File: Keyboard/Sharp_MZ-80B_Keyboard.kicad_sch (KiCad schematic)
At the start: 98 parts, among them J1 Tape Controls, J2 Keyboard Matrix, J3 LEDs, SW1 CMT_EJECT, SW10 CLR HOME, SW11 INST DEL, SW12 8, SW13 9, SW14 COLON, SW15 SEMI COLON, SW16 -, SW17 @, SW18 [, SW19 0, SW2 CMT_FF, SW20 1, SW21 2, SW22 3, SW23 4, SW24 5, SW25 6, SW26 7, SW27 X, SW28 Y, SW29 Z, SW3 CMT_REW, SW30 ^, SW31 \, SW32 ?, SW33 DOT, SW34 COMMA, SW35 P, SW36 Q, SW37 R, SW38 S, SW39 T, SW4 CMT_STOP, SW40 U, SW41 V, SW42 W, SW43 I, SW44 H, SW45 J, SW46 K, SW47 L, SW48 M, SW49 N, SW5 GRPH, SW50 O, SW51 /, SW52 A, SW53 B, SW54 C, SW55 D, SW56 E, SW57 F, SW58 G, SW59 TAB, SW6 SFT LOCK, SW60 SPACE, SW61 CR, SW62 UP, SW63 DOWN, SW64 LEFT, SW65 RIGHT, SW66 BREAK, SW67 NP 0, SW68 NP 1, SW69 NP 2, SW7 RH SHIFT, SW70 NP 3, SW71 NP 4, SW72 NP 5, SW73 NP 6, SW74 NP 7, SW75 F9, SW76 F10, SW77 NP 8, SW78 NP 9, SW79 NP 00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

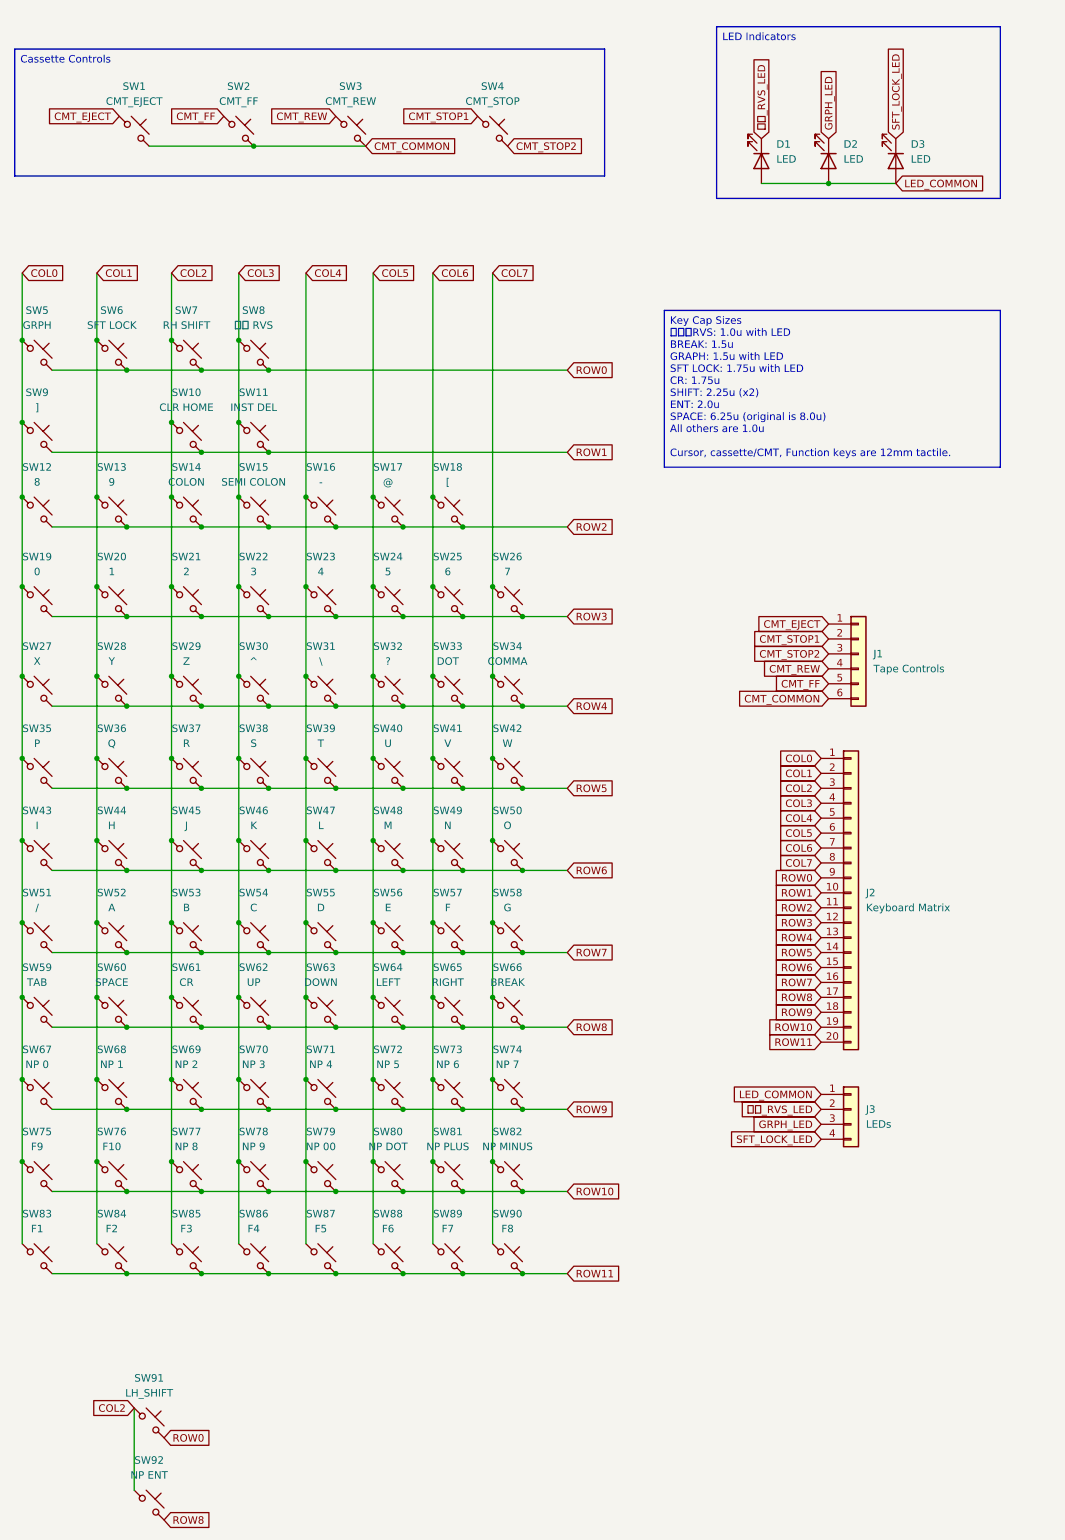
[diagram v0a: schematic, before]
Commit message: Schematic updates
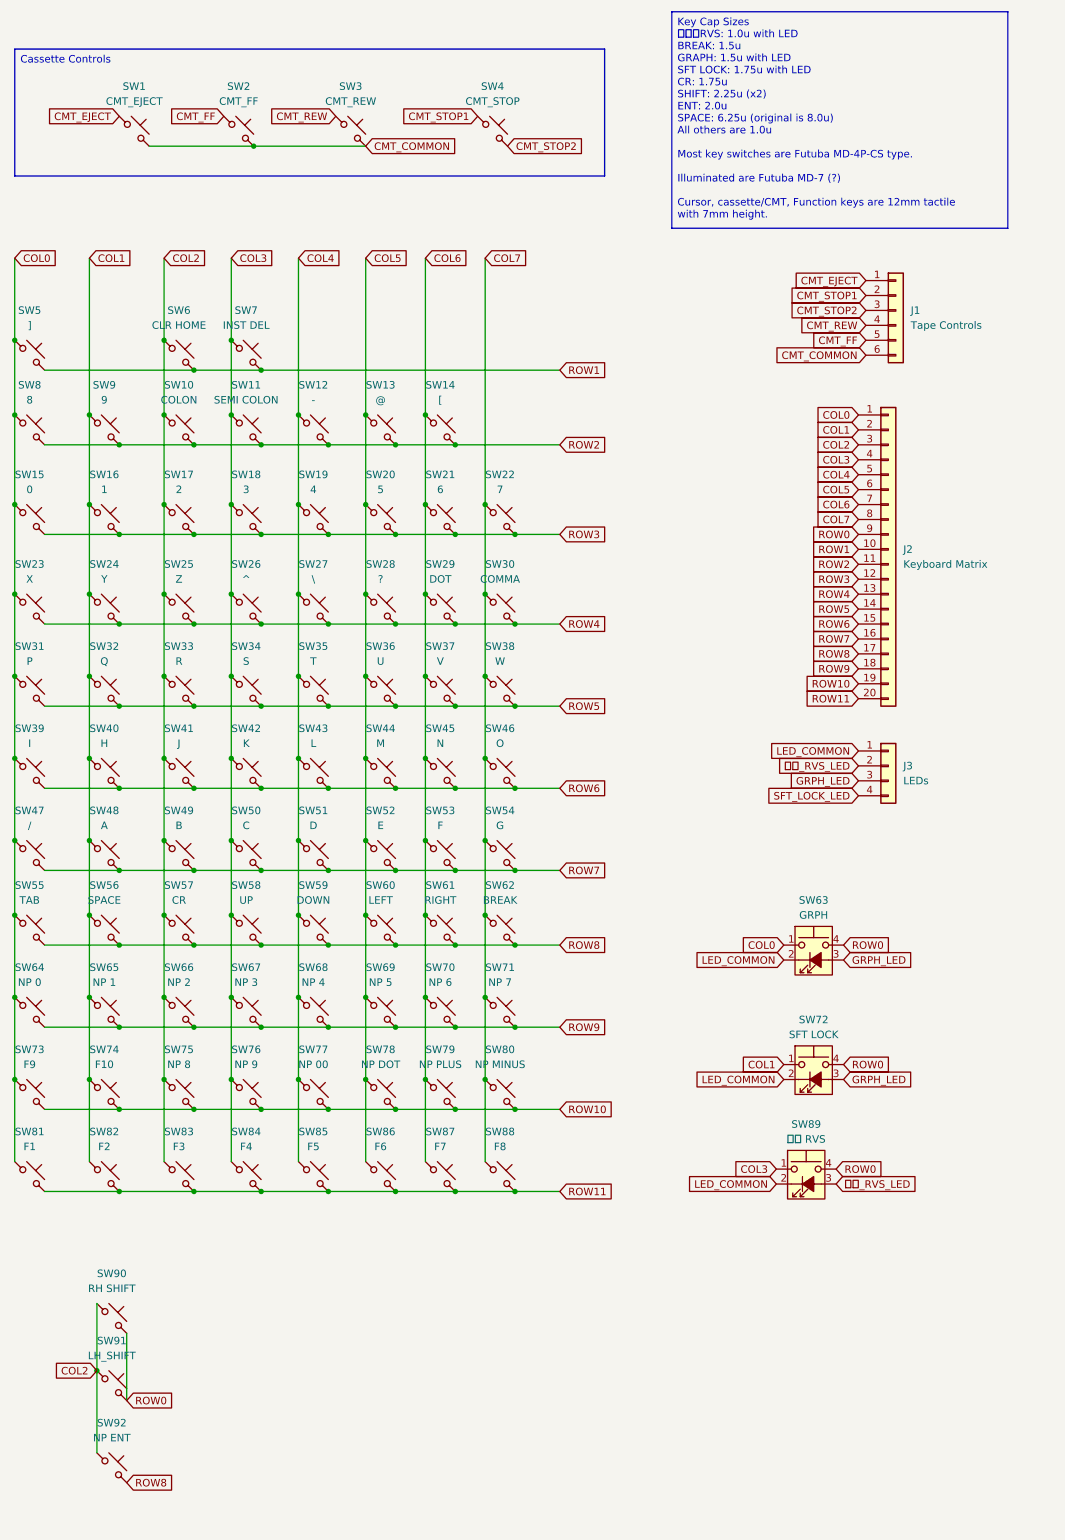
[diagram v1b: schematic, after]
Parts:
- removed D1, D2, D3: LED, LED_THT:LED_D5.0mm, symbol Device:LED
- removed SW5: GRPH, PCM_Switch_Keyboard_Cherry_MX:SW_Cherry_MX_Plate_1.50u, symbol Switch:SW_Push_45deg
- removed SW6: SFT LOCK, PCM_Switch_Keyboard_Cherry_MX:SW_Cherry_MX_Plate_1.75u, symbol Switch:SW_Push_45deg
- removed SW8: カナ RVS, PCM_Switch_Keyboard_Cherry_MX:SW_Cherry_MX_Plate_1.00u, symbol Switch:SW_Push_45deg
- added SW63: GRPH, Clueless_Engineer:Futuba MD-7, symbol Switch:SW_MEC_5G_LED
- added SW72: SFT LOCK, Clueless_Engineer:Futuba MD-7, symbol Switch:SW_MEC_5G_LED
- added SW89: カナ RVS, Clueless_Engineer:Futuba MD-7, symbol Switch:SW_MEC_5G_LED
- SW10: renamed from SW14; footprint PCM_Switch_Keyboard_Cherry_MX:SW_Cherry_MX_Plate_1.00u -> Clueless_Engineer:Futuba MD-4P
- SW11: renamed from SW15; footprint PCM_Switch_Keyboard_Cherry_MX:SW_Cherry_MX_Plate_1.00u -> Clueless_Engineer:Futuba MD-4P
- SW12: renamed from SW16; footprint PCM_Switch_Keyboard_Cherry_MX:SW_Cherry_MX_Plate_1.00u -> Clueless_Engineer:Futuba MD-4P
- SW13: renamed from SW17; footprint PCM_Switch_Keyboard_Cherry_MX:SW_Cherry_MX_Plate_1.00u -> Clueless_Engineer:Futuba MD-4P
- SW14: renamed from SW18; footprint PCM_Switch_Keyboard_Cherry_MX:SW_Cherry_MX_Plate_1.00u -> Clueless_Engineer:Futuba MD-4P
- SW15: renamed from SW19; footprint PCM_Switch_Keyboard_Cherry_MX:SW_Cherry_MX_Plate_1.00u -> Clueless_Engineer:Futuba MD-4P
- SW16: renamed from SW20; footprint PCM_Switch_Keyboard_Cherry_MX:SW_Cherry_MX_Plate_1.00u -> Clueless_Engineer:Futuba MD-4P
- SW17: renamed from SW21; footprint PCM_Switch_Keyboard_Cherry_MX:SW_Cherry_MX_Plate_1.00u -> Clueless_Engineer:Futuba MD-4P
- SW18: renamed from SW22; footprint PCM_Switch_Keyboard_Cherry_MX:SW_Cherry_MX_Plate_1.00u -> Clueless_Engineer:Futuba MD-4P
- SW19: renamed from SW23; footprint PCM_Switch_Keyboard_Cherry_MX:SW_Cherry_MX_Plate_1.00u -> Clueless_Engineer:Futuba MD-4P
- SW20: renamed from SW24; footprint PCM_Switch_Keyboard_Cherry_MX:SW_Cherry_MX_Plate_1.00u -> Clueless_Engineer:Futuba MD-4P
- SW21: renamed from SW25; footprint PCM_Switch_Keyboard_Cherry_MX:SW_Cherry_MX_Plate_1.00u -> Clueless_Engineer:Futuba MD-4P
- SW22: renamed from SW26; footprint PCM_Switch_Keyboard_Cherry_MX:SW_Cherry_MX_Plate_1.00u -> Clueless_Engineer:Futuba MD-4P
- SW23: renamed from SW27; footprint PCM_Switch_Keyboard_Cherry_MX:SW_Cherry_MX_Plate_1.00u -> Clueless_Engineer:Futuba MD-4P
- SW24: renamed from SW28; footprint PCM_Switch_Keyboard_Cherry_MX:SW_Cherry_MX_Plate_1.00u -> Clueless_Engineer:Futuba MD-4P
- SW25: renamed from SW29; footprint PCM_Switch_Keyboard_Cherry_MX:SW_Cherry_MX_Plate_1.00u -> Clueless_Engineer:Futuba MD-4P
- SW26: renamed from SW30; footprint PCM_Switch_Keyboard_Cherry_MX:SW_Cherry_MX_Plate_1.00u -> Clueless_Engineer:Futuba MD-4P
- SW27: renamed from SW31; footprint PCM_Switch_Keyboard_Cherry_MX:SW_Cherry_MX_Plate_1.00u -> Clueless_Engineer:Futuba MD-4P
- SW28: renamed from SW32; footprint PCM_Switch_Keyboard_Cherry_MX:SW_Cherry_MX_Plate_1.00u -> Clueless_Engineer:Futuba MD-4P
- SW29: renamed from SW33; footprint PCM_Switch_Keyboard_Cherry_MX:SW_Cherry_MX_Plate_1.00u -> Clueless_Engineer:Futuba MD-4P
- SW30: renamed from SW34; footprint PCM_Switch_Keyboard_Cherry_MX:SW_Cherry_MX_Plate_1.00u -> Clueless_Engineer:Futuba MD-4P
- SW31: renamed from SW35; footprint PCM_Switch_Keyboard_Cherry_MX:SW_Cherry_MX_Plate_1.00u -> Clueless_Engineer:Futuba MD-4P
- SW32: renamed from SW36; footprint PCM_Switch_Keyboard_Cherry_MX:SW_Cherry_MX_Plate_1.00u -> Clueless_Engineer:Futuba MD-4P
- SW33: renamed from SW37; footprint PCM_Switch_Keyboard_Cherry_MX:SW_Cherry_MX_Plate_1.00u -> Clueless_Engineer:Futuba MD-4P
- SW34: renamed from SW38; footprint PCM_Switch_Keyboard_Cherry_MX:SW_Cherry_MX_Plate_1.00u -> Clueless_Engineer:Futuba MD-4P
- SW35: renamed from SW39; footprint PCM_Switch_Keyboard_Cherry_MX:SW_Cherry_MX_Plate_1.00u -> Clueless_Engineer:Futuba MD-4P
- SW36: renamed from SW40; footprint PCM_Switch_Keyboard_Cherry_MX:SW_Cherry_MX_Plate_1.00u -> Clueless_Engineer:Futuba MD-4P
- SW37: renamed from SW41; footprint PCM_Switch_Keyboard_Cherry_MX:SW_Cherry_MX_Plate_1.00u -> Clueless_Engineer:Futuba MD-4P
- SW38: renamed from SW42; footprint PCM_Switch_Keyboard_Cherry_MX:SW_Cherry_MX_Plate_1.00u -> Clueless_Engineer:Futuba MD-4P
- SW39: renamed from SW43; footprint PCM_Switch_Keyboard_Cherry_MX:SW_Cherry_MX_Plate_1.00u -> Clueless_Engineer:Futuba MD-4P
- SW40: renamed from SW44; footprint PCM_Switch_Keyboard_Cherry_MX:SW_Cherry_MX_Plate_1.00u -> Clueless_Engineer:Futuba MD-4P
- SW41: renamed from SW45; footprint PCM_Switch_Keyboard_Cherry_MX:SW_Cherry_MX_Plate_1.00u -> Clueless_Engineer:Futuba MD-4P
- SW42: renamed from SW46; footprint PCM_Switch_Keyboard_Cherry_MX:SW_Cherry_MX_Plate_1.00u -> Clueless_Engineer:Futuba MD-4P
- SW43: renamed from SW47; footprint PCM_Switch_Keyboard_Cherry_MX:SW_Cherry_MX_Plate_1.00u -> Clueless_Engineer:Futuba MD-4P
- SW44: renamed from SW48; footprint PCM_Switch_Keyboard_Cherry_MX:SW_Cherry_MX_Plate_1.00u -> Clueless_Engineer:Futuba MD-4P
- SW45: renamed from SW49; footprint PCM_Switch_Keyboard_Cherry_MX:SW_Cherry_MX_Plate_1.00u -> Clueless_Engineer:Futuba MD-4P
- SW46: renamed from SW50; footprint PCM_Switch_Keyboard_Cherry_MX:SW_Cherry_MX_Plate_1.00u -> Clueless_Engineer:Futuba MD-4P
- SW47: renamed from SW51; footprint PCM_Switch_Keyboard_Cherry_MX:SW_Cherry_MX_Plate_1.00u -> Clueless_Engineer:Futuba MD-4P
- SW48: renamed from SW52; footprint PCM_Switch_Keyboard_Cherry_MX:SW_Cherry_MX_Plate_1.00u -> Clueless_Engineer:Futuba MD-4P
- SW49: renamed from SW53; footprint PCM_Switch_Keyboard_Cherry_MX:SW_Cherry_MX_Plate_1.00u -> Clueless_Engineer:Futuba MD-4P
- SW5: renamed from SW9; footprint PCM_Switch_Keyboard_Cherry_MX:SW_Cherry_MX_Plate_1.00u -> Clueless_Engineer:Futuba MD-4P
- SW50: renamed from SW54; footprint PCM_Switch_Keyboard_Cherry_MX:SW_Cherry_MX_Plate_1.00u -> Clueless_Engineer:Futuba MD-4P
- SW51: renamed from SW55; footprint PCM_Switch_Keyboard_Cherry_MX:SW_Cherry_MX_Plate_1.00u -> Clueless_Engineer:Futuba MD-4P
- SW52: renamed from SW56; footprint PCM_Switch_Keyboard_Cherry_MX:SW_Cherry_MX_Plate_1.00u -> Clueless_Engineer:Futuba MD-4P
- SW53: renamed from SW57; footprint PCM_Switch_Keyboard_Cherry_MX:SW_Cherry_MX_Plate_1.00u -> Clueless_Engineer:Futuba MD-4P
- SW54: renamed from SW58; footprint PCM_Switch_Keyboard_Cherry_MX:SW_Cherry_MX_Plate_1.00u -> Clueless_Engineer:Futuba MD-4P
- SW55: renamed from SW59; footprint PCM_Switch_Keyboard_Cherry_MX:SW_Cherry_MX_Plate_1.00u -> Clueless_Engineer:Futuba MD-4P
- SW56: renamed from SW60; footprint PCM_Switch_Keyboard_Cherry_MX:SW_Cherry_MX_Plate_6.25u -> Clueless_Engineer:Futuba MD-4P
- SW57: renamed from SW61; footprint PCM_Switch_Keyboard_Cherry_MX:SW_Cherry_MX_Plate_1.75u -> Clueless_Engineer:Futuba MD-4P
- SW6: renamed from SW10; footprint PCM_Switch_Keyboard_Cherry_MX:SW_Cherry_MX_Plate_1.00u -> Clueless_Engineer:Futuba MD-4P
- SW62: renamed from SW66; footprint PCM_Switch_Keyboard_Cherry_MX:SW_Cherry_MX_Plate_1.50u -> Clueless_Engineer:Futuba MD-4P
- SW64: renamed from SW67; footprint PCM_Switch_Keyboard_Cherry_MX:SW_Cherry_MX_Plate_1.00u -> Clueless_Engineer:Futuba MD-4P
- SW65: renamed from SW68; footprint PCM_Switch_Keyboard_Cherry_MX:SW_Cherry_MX_Plate_1.00u -> Clueless_Engineer:Futuba MD-4P
- SW66: renamed from SW69; footprint PCM_Switch_Keyboard_Cherry_MX:SW_Cherry_MX_Plate_1.00u -> Clueless_Engineer:Futuba MD-4P
- SW67: renamed from SW70; footprint PCM_Switch_Keyboard_Cherry_MX:SW_Cherry_MX_Plate_1.00u -> Clueless_Engineer:Futuba MD-4P
- SW68: renamed from SW71; footprint PCM_Switch_Keyboard_Cherry_MX:SW_Cherry_MX_Plate_1.00u -> Clueless_Engineer:Futuba MD-4P
- SW69: renamed from SW72; footprint PCM_Switch_Keyboard_Cherry_MX:SW_Cherry_MX_Plate_1.00u -> Clueless_Engineer:Futuba MD-4P
- SW7: renamed from SW11; footprint PCM_Switch_Keyboard_Cherry_MX:SW_Cherry_MX_Plate_1.00u -> Clueless_Engineer:Futuba MD-4P
- SW70: renamed from SW73; footprint PCM_Switch_Keyboard_Cherry_MX:SW_Cherry_MX_Plate_1.00u -> Clueless_Engineer:Futuba MD-4P
- SW71: renamed from SW74; footprint PCM_Switch_Keyboard_Cherry_MX:SW_Cherry_MX_Plate_1.00u -> Clueless_Engineer:Futuba MD-4P
- SW75: renamed from SW77; footprint PCM_Switch_Keyboard_Cherry_MX:SW_Cherry_MX_Plate_1.00u -> Clueless_Engineer:Futuba MD-4P
- SW76: renamed from SW78; footprint PCM_Switch_Keyboard_Cherry_MX:SW_Cherry_MX_Plate_1.00u -> Clueless_Engineer:Futuba MD-4P
- SW77: renamed from SW79; footprint PCM_Switch_Keyboard_Cherry_MX:SW_Cherry_MX_Plate_1.00u -> Clueless_Engineer:Futuba MD-4P
- SW78: renamed from SW80; footprint PCM_Switch_Keyboard_Cherry_MX:SW_Cherry_MX_Plate_1.00u -> Clueless_Engineer:Futuba MD-4P
- SW79: renamed from SW81; footprint PCM_Switch_Keyboard_Cherry_MX:SW_Cherry_MX_Plate_1.00u -> Clueless_Engineer:Futuba MD-4P
- SW8: renamed from SW12; footprint PCM_Switch_Keyboard_Cherry_MX:SW_Cherry_MX_Plate_1.00u -> Clueless_Engineer:Futuba MD-4P
- SW80: renamed from SW82; footprint PCM_Switch_Keyboard_Cherry_MX:SW_Cherry_MX_Plate_1.00u -> Clueless_Engineer:Futuba MD-4P
- SW9: renamed from SW13; footprint PCM_Switch_Keyboard_Cherry_MX:SW_Cherry_MX_Plate_1.00u -> Clueless_Engineer:Futuba MD-4P
- SW90: renamed from SW7; footprint PCM_Switch_Keyboard_Cherry_MX:SW_Cherry_MX_Plate_2.25u -> Clueless_Engineer:Futuba MD-4P
- SW91: footprint PCM_Switch_Keyboard_Cherry_MX:SW_Cherry_MX_Plate_2.25u -> Clueless_Engineer:Futuba MD-4P
- SW92: footprint PCM_Switch_Keyboard_Cherry_MX:SW_Cherry_MX_Plate_2.00u_90deg -> Clueless_Engineer:Futuba MD-4P
- renumbered SW62 to SW58, SW63 to SW59, SW64 to SW60, SW65 to SW61, SW75 to SW73, SW76 to SW74, SW83 to SW81, SW84 to SW82, SW85 to SW83, SW86 to SW84, SW87 to SW85, SW88 to SW86, SW89 to SW87, SW90 to SW88
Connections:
- net COL0: now also SW63.1
- net COL1: now also SW72.1
- net COL3: now also SW89.1
- net GRPH_LED: now also SW63.3 (K), SW72.3 (K)
- net LED_COMMON: now also SW63.2, SW72.2, SW89.2
- net ROW0: now also SW63.4 (A), SW72.4 (A), SW89.4 (A)
- net カナ_RVS_LED: now also SW89.3 (K)
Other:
- moved on the sheet: J1, J2, J3, SW10, SW11, SW12, SW13, SW14, SW15, SW16, SW17, SW18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

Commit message: Initial design
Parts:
- SW15: value 0 -> ZERO
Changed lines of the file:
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@@
 		)
 	)
-	(text_box "Key Cap Sizes\nカナ　RVS: 1.0u with LED\nBREAK: 1.5u\nGRAPH: 1.5u with LED\nSFT LOCK: 1.75u with LED\nCR: 1.75u\nSHIFT: 2.25u (x2)\nENT: 2.0u\nSPACE: 6.25u (original is 8.0u)\nAll others are 1.0u\n\nMost key switches are Futuba MD-4P-CS type.\n\nIlluminated are Futuba MD-7 (?)\n\nCursor, cassette/CMT, Function keys are 12mm tactile with 7mm height."
+	(text_box "Key Cap Sizes\nカナ　RVS: 1.0u with LED\nBREAK: 1.5u\nGRAPH: 1.5u with LED\nSFT LOCK: 1.75u with LED\nCR: 1.75u\nSHIFT: 2.25u (x2)\nENT: 2.0u\nSPACE: 8.0u\nAll others are 1.0u\n\nMost key switches are Futuba MD-4P-CS type.\n\nIlluminated are Futuba MD-7 (?)\n\nCursor, cassette/CMT, Function keys are 12mm tactile with 7mm height."
 		(exclude_from_sim no)
 		(at 138.43 13.97 0)
@@
 			)
 		)
-		(property "Value" "0"
+		(property "Value" "ZERO"
 			(at 29.21 95.25 0)
 			(effects

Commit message: Keyboard design progress
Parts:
- added H1, H2, H3, H4, H5: MountingHole, MountingHole:MountingHole_4.3mm_M4, symbol Mechanical:MountingHole
- added H6, H7, H8, H9: MountingHole, MountingHole:MountingHole_3.2mm_M3, symbol Mechanical:MountingHole
